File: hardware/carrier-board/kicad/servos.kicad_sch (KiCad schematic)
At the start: 0 parts

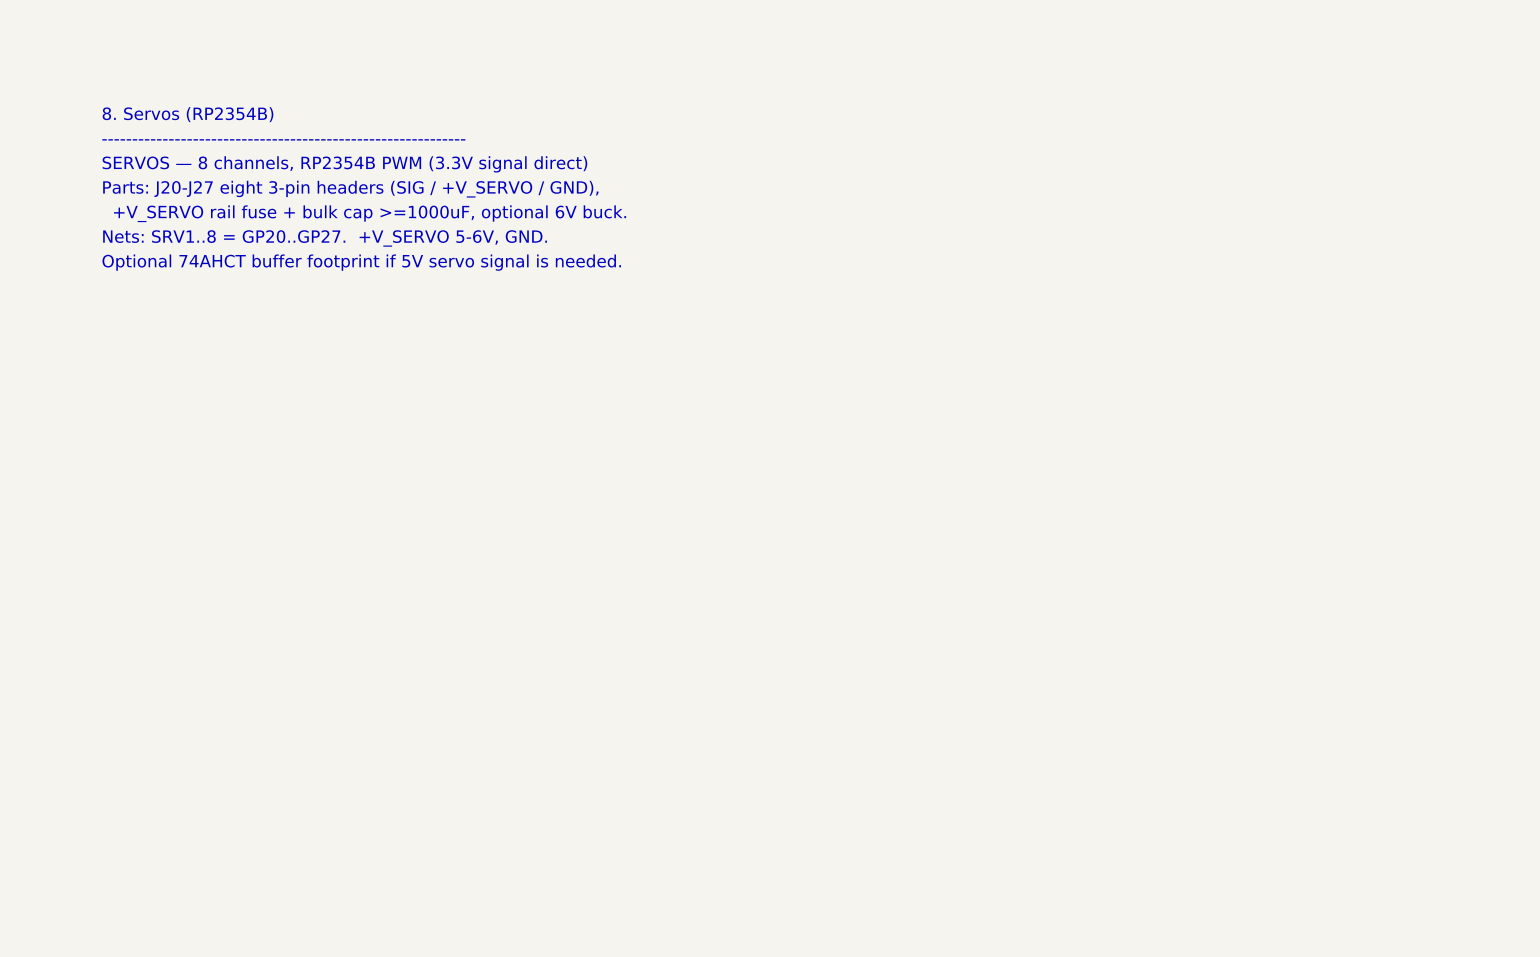
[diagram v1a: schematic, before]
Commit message: Carrier KiCad: populate all 11 schematic sheets
Replace populate_face_buffer.py with populate_sheets.py: one generator that
emits all 11 populated sub-sheets reusing the KiCad-9 format proven by the
face_buffer proof. Shared symbol library + generic box-symbol builder; condensed
CM5 (2x DF40-100) and RP2354B (QFN-80) symbols showing only used pins.

Connectivity by net labels (global for rails + cross-sheet nets: GPIOxx HUB75,
MX_*, LED*_DAT, SRV*, BTN*, *_USB_*; local within-sheet). Sheets: power
(protection + rails + AP2112 +3V3_RP), cm5 (HUB75 out + fan MOSFETs + RP ctrl),
face_buffer, rp2354_io (RP2354B + xtal + SW1/J12 + ESD + SWD), rp2354_face
(U10->J3), leds (U11 quad ->J4a-d), sensors_i2c (pull-ups+J5+STEMMA),
servos (J20-27 + rail), gpio_buttons (J6), usb (USB2514B hub + uplink),
cameras_display (CSI FFC + HDMI).

Verified: all sheets paren-balanced, every used lib_id defined, all instance
paths match sheet UUIDs, root<->sub-sheet UUID linkage intact. generate_skeleton.py
now lists all sheets POPULATED (writes only root+project). Not yet opened in
KiCad here -- expect ERC warnings (PWR_FLAG, unconnected pins) to clean.
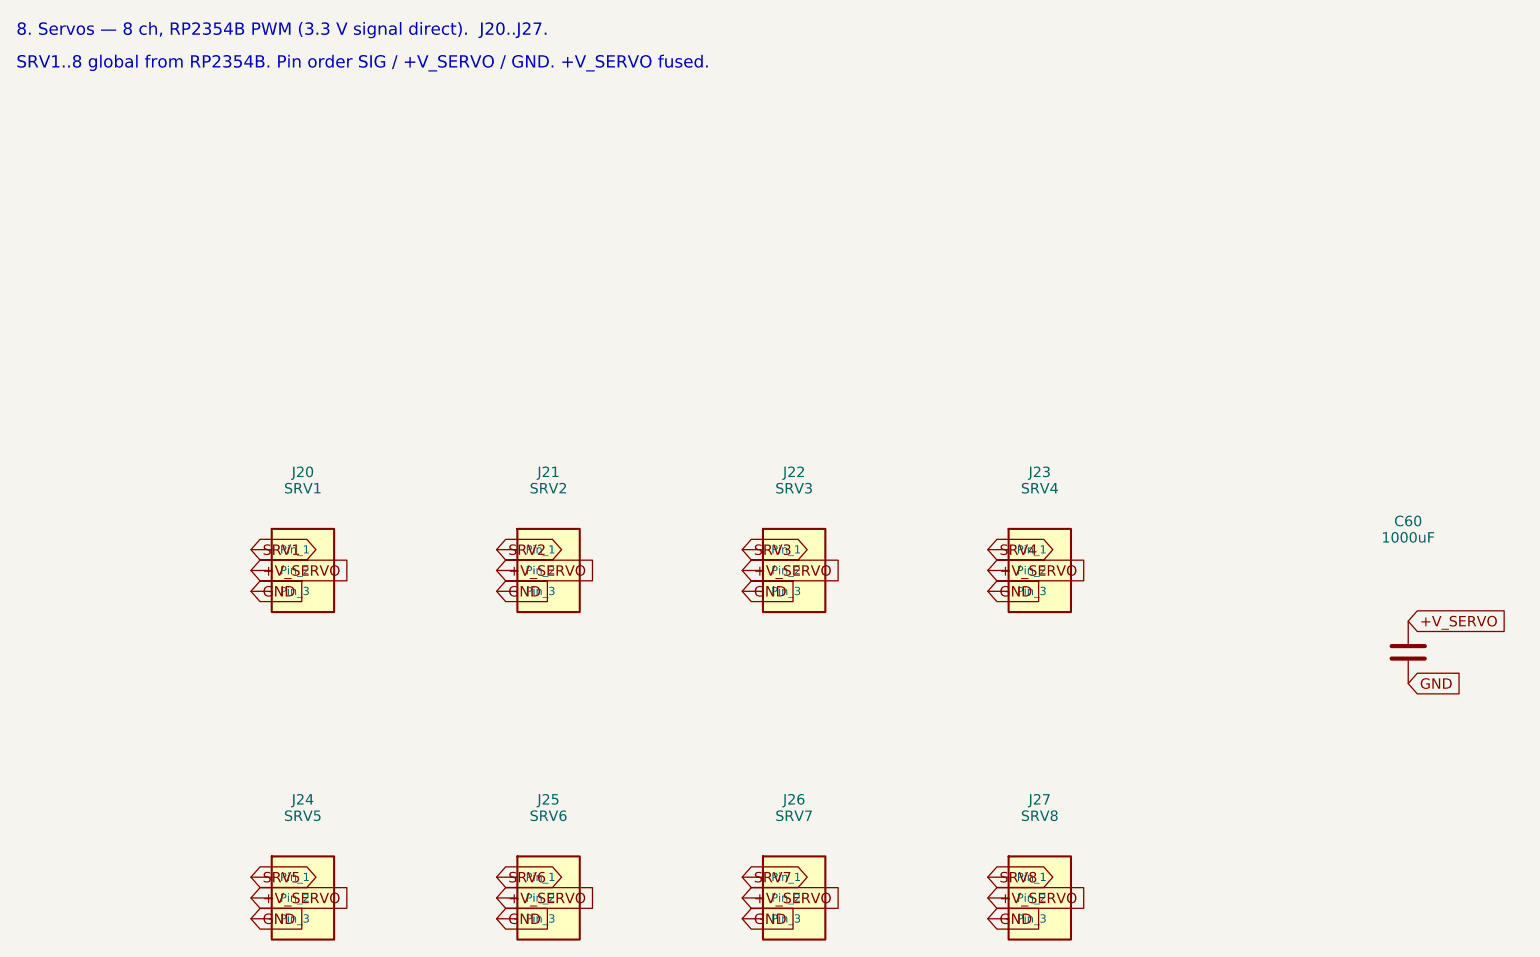
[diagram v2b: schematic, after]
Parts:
- added C60: 1000uF, symbol Device:C
- added J20: SRV1, symbol Connector_Generic:Conn_01x03
- added J21: SRV2, symbol Connector_Generic:Conn_01x03
- added J22: SRV3, symbol Connector_Generic:Conn_01x03
- added J23: SRV4, symbol Connector_Generic:Conn_01x03
- added J24: SRV5, symbol Connector_Generic:Conn_01x03
- added J25: SRV6, symbol Connector_Generic:Conn_01x03
- added J26: SRV7, symbol Connector_Generic:Conn_01x03
- added J27: SRV8, symbol Connector_Generic:Conn_01x03
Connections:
- new net +V_SERVO: C60.1, J20.2 (Pin_2), J21.2 (Pin_2), J22.2 (Pin_2), J23.2 (Pin_2), J24.2 (Pin_2), J25.2 (Pin_2), J26.2 (Pin_2), J27.2 (Pin_2)
- new net GND: C60.2, J20.3 (Pin_3), J21.3 (Pin_3), J22.3 (Pin_3), J23.3 (Pin_3), J24.3 (Pin_3), J25.3 (Pin_3), J26.3 (Pin_3), J27.3 (Pin_3)
- new net SRV1: J20.1 (Pin_1)
- new net SRV2: J21.1 (Pin_1)
- new net SRV3: J22.1 (Pin_1)
- new net SRV4: J23.1 (Pin_1)
- new net SRV5: J24.1 (Pin_1)
- new net SRV6: J25.1 (Pin_1)
- new net SRV7: J26.1 (Pin_1)
- new net SRV8: J27.1 (Pin_1)
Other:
- note added: "8. Servos — 8 ch, RP2354B PWM (3.3 V signal direct). J20..J27."
- note added: "SRV1..8 global from RP2354B. Pin order SIG / +V_SERVO / GND. +V_SERVO fused."
- note removed: "+V_SERVO rail fuse + bulk cap >=1000uF, optional 6V buck."
- note removed: "------------------------------------------------------------"
- note removed: "8. Servos (RP2354B)"
- note removed: "Nets: SRV1..8 = GP20..GP27. +V_SERVO 5-6V, GND."
- note removed: "Optional 74AHCT buffer footprint if 5V servo signal is needed."
- note removed: "Parts: J20-J27 eight 3-pin headers (SIG / +V_SERVO / GND),"
- note removed: "SERVOS — 8 channels, RP2354B PWM (3.3V signal direct)"
